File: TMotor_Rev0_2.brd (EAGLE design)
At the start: 106.7 x 74.3 mm, 86 parts, among them J1 5015680507, J10 5015680207, J2 5015680507, J7 5015680207, J8 5015680207, J9 5015680207, Q1 IRLB8721PBFTO220H, Q2 IRLB8721PBFTO220H, Q3 IRLB8721PBFTO220H, Q4 IRLB8721PBFTO220H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

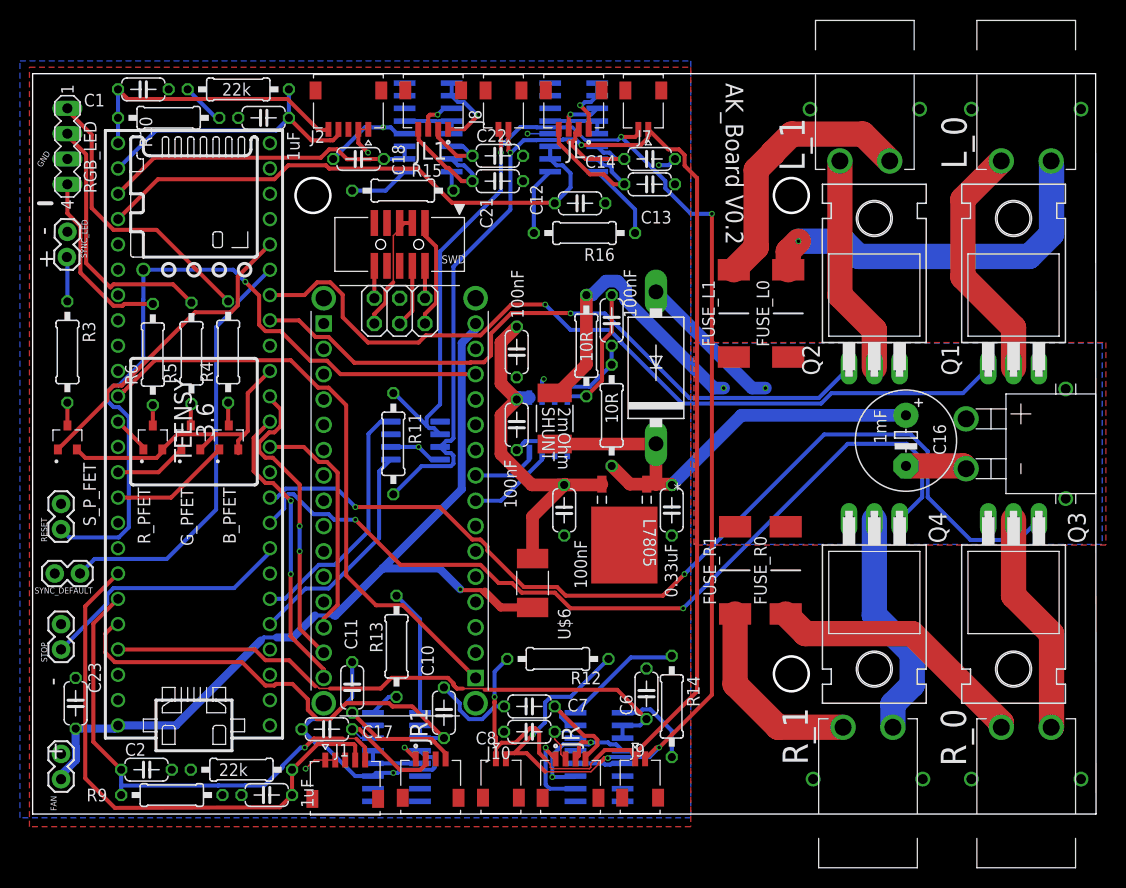
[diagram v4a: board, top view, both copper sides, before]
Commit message: Added Estop to motor power circuit
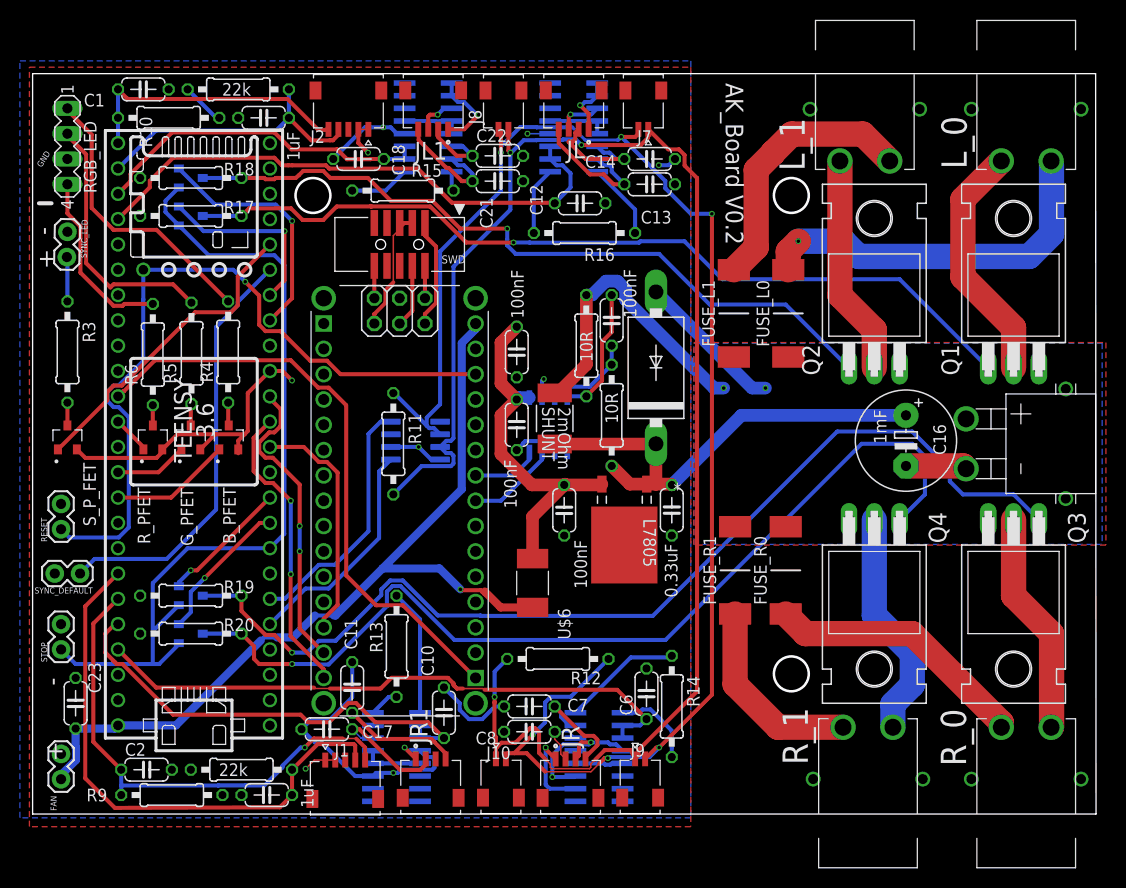
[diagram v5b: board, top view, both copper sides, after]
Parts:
- added R17, R18, R19, R20: 10R, rcl:0207/10
- added U6, U7, U8, U9: 2SJ305TE85LF, 2SJ305TE85LF:TRANS_SSM3J325F,LF
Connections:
- new net L0_ENABLE_STOP: Q1.1, R17.2, U6.3
- new net L1_ENABLE_STOP: Q2.1, R18.2, U7.3
- new net R0_ENABLE_STOP: Q3.1, R19.2, U8.3
- new net R1_ENABLE_STOP: Q4.1, R20.2, U9.3
- net GND: now also R17.1, R18.1, R19.1, R20.1
- net L_0_ENABLE: now also U6.2; no longer Q1.1
- net L_1_ENABLE: now also U7.2; no longer Q2.1
- net R_0_ENABLE: now also U8.2; no longer Q3.1
- net R_1_ENABLE: now also U9.2; no longer Q4.1
- net STOP: now also U6.1, U7.1, U8.1, U9.1
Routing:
- net R0_ENABLE_STOP: track 0.00 -> 104.0 mm, vias 0 -> 1
- net R1_ENABLE_STOP: track 0.00 -> 96.9 mm, vias 0 -> 1
- net L0_ENABLE_STOP: track 0.00 -> 87.1 mm, vias 0 -> 1
- net R_0_ENABLE: track 96.8 -> 13.0 mm, vias 2 -> 1
- net L1_ENABLE_STOP: track 0.00 -> 74.4 mm, vias 0 -> 1
- net R_1_ENABLE: track 86.5 -> 14.5 mm, vias 2 -> 1
- net L_0_ENABLE: track 83.7 -> 18.6 mm
- net STOP: track 25.9 -> 84.5 mm
- net L_1_ENABLE: track 68.0 -> 24.4 mm
- net TRQ_AMP_R1: track 69.0 -> 48.4 mm
- net 3.3V: track 62.1 -> 64.7 mm, vias 6 -> 7
- net TRQ_AMP_L1: track 32.3 -> 34.1 mm
- net TRQ_AMP_L: track 55.2 -> 56.2 mm
- net VIN: track 37.0 -> 36.4 mm

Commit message: Updated resistor value on motor stop pulldown
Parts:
- R17, R18: value 10R -> 1K
- R19, R20: value 10R -> 1k
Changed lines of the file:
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@@
 <attribute name="VALUE" x="-20.32" y="29.21" size="1.27" layer="28" rot="MR180"/>
 </element>
-<element name="R17" library="rcl" library_urn="urn:adsk.eagle:library:334" package="0207/10" package3d_urn="urn:adsk.eagle:package:23491/2" value="10R" x="-17.78" y="67.31" smashed="yes">
+<element name="R17" library="rcl" library_urn="urn:adsk.eagle:library:334" package="0207/10" package3d_urn="urn:adsk.eagle:package:23491/2" value="1K" x="-17.78" y="67.31" smashed="yes">
 <attribute name="NAME" x="-14.478" y="67.564" size="1.27" layer="25" ratio="10"/>
 <attribute name="POPULARITY" value="36" x="-17.78" y="67.31" size="1.778" layer="27" display="off"/>
@@
 <attribute name="VALUE" x="-20.0406" y="66.675" size="1.27" layer="27" ratio="10"/>
 </element>
-<element name="R18" library="rcl" library_urn="urn:adsk.eagle:library:334" package="0207/10" package3d_urn="urn:adsk.eagle:package:23491/2" value="10R" x="-17.78" y="71.12" smashed="yes">
+<element name="R18" library="rcl" library_urn="urn:adsk.eagle:library:334" package="0207/10" package3d_urn="urn:adsk.eagle:package:23491/2" value="1K" x="-17.78" y="71.12" smashed="yes">
 <attribute name="NAME" x="-14.478" y="71.374" size="1.27" layer="25" ratio="10"/>
 <attribute name="POPULARITY" value="36" x="-17.78" y="71.12" size="1.778" layer="27" display="off"/>
@@
 <attribute name="VALUE" x="-20.0406" y="70.485" size="1.27" layer="27" ratio="10"/>
 </element>
-<element name="R19" library="rcl" library_urn="urn:adsk.eagle:library:334" package="0207/10" package3d_urn="urn:adsk.eagle:package:23491/2" value="10R" x="-17.78" y="29.21" smashed="yes">
+<element name="R19" library="rcl" library_urn="urn:adsk.eagle:library:334" package="0207/10" package3d_urn="urn:adsk.eagle:package:23491/2" value="1k" x="-17.78" y="29.21" smashed="yes">
 <attribute name="NAME" x="-14.478" y="29.464" size="1.27" layer="25" ratio="10"/>
 <attribute name="POPULARITY" value="36" x="-17.78" y="29.21" size="1.778" layer="27" display="off"/>
@@
 <attribute name="VALUE" x="-20.0406" y="28.575" size="1.27" layer="27" ratio="10"/>
 </element>
-<element name="R20" library="rcl" library_urn="urn:adsk.eagle:library:334" package="0207/10" package3d_urn="urn:adsk.eagle:package:23491/2" value="10R" x="-17.78" y="25.4" smashed="yes">
+<element name="R20" library="rcl" library_urn="urn:adsk.eagle:library:334" package="0207/10" package3d_urn="urn:adsk.eagle:package:23491/2" value="1k" x="-17.78" y="25.4" smashed="yes">
 <attribute name="NAME" x="-14.478" y="25.654" size="1.27" layer="25" ratio="10"/>
 <attribute name="POPULARITY" value="36" x="-17.78" y="25.4" size="1.778" layer="27" display="off"/>

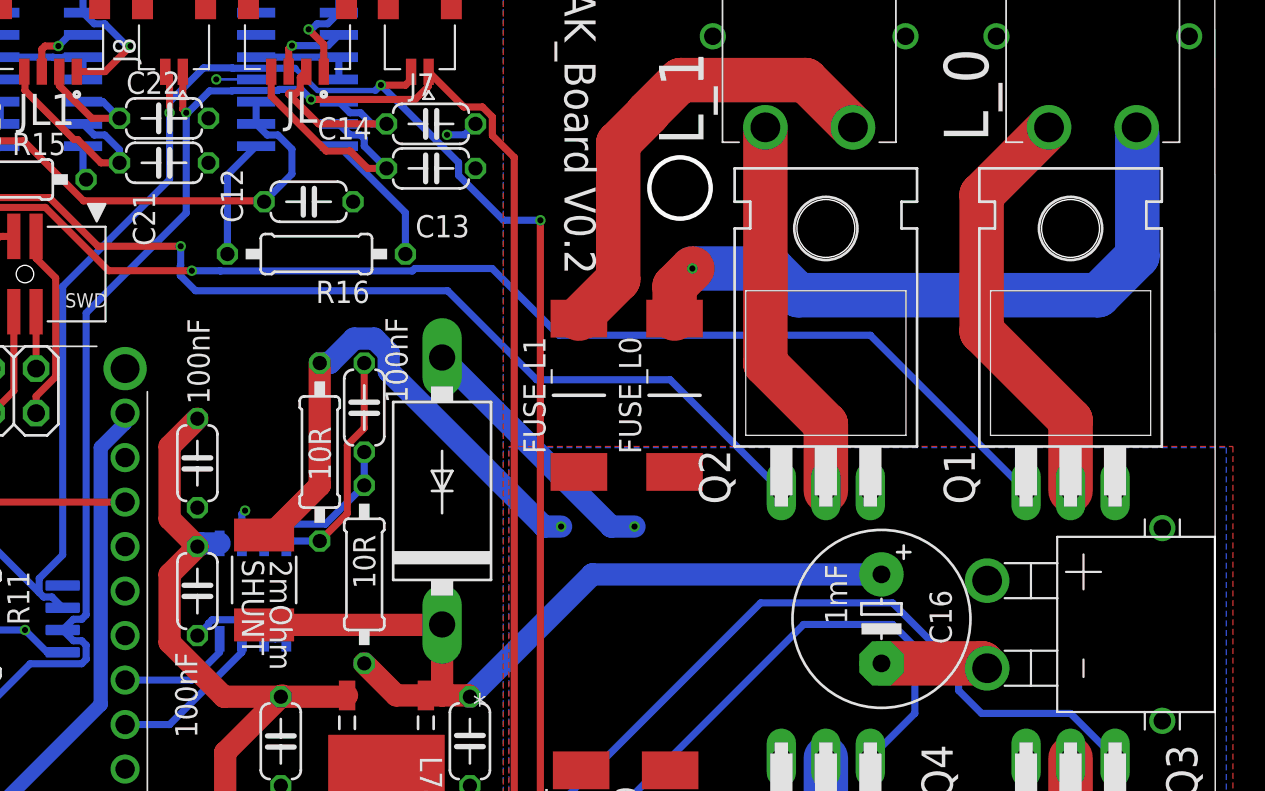
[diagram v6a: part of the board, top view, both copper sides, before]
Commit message: rerouted some traces for motor power
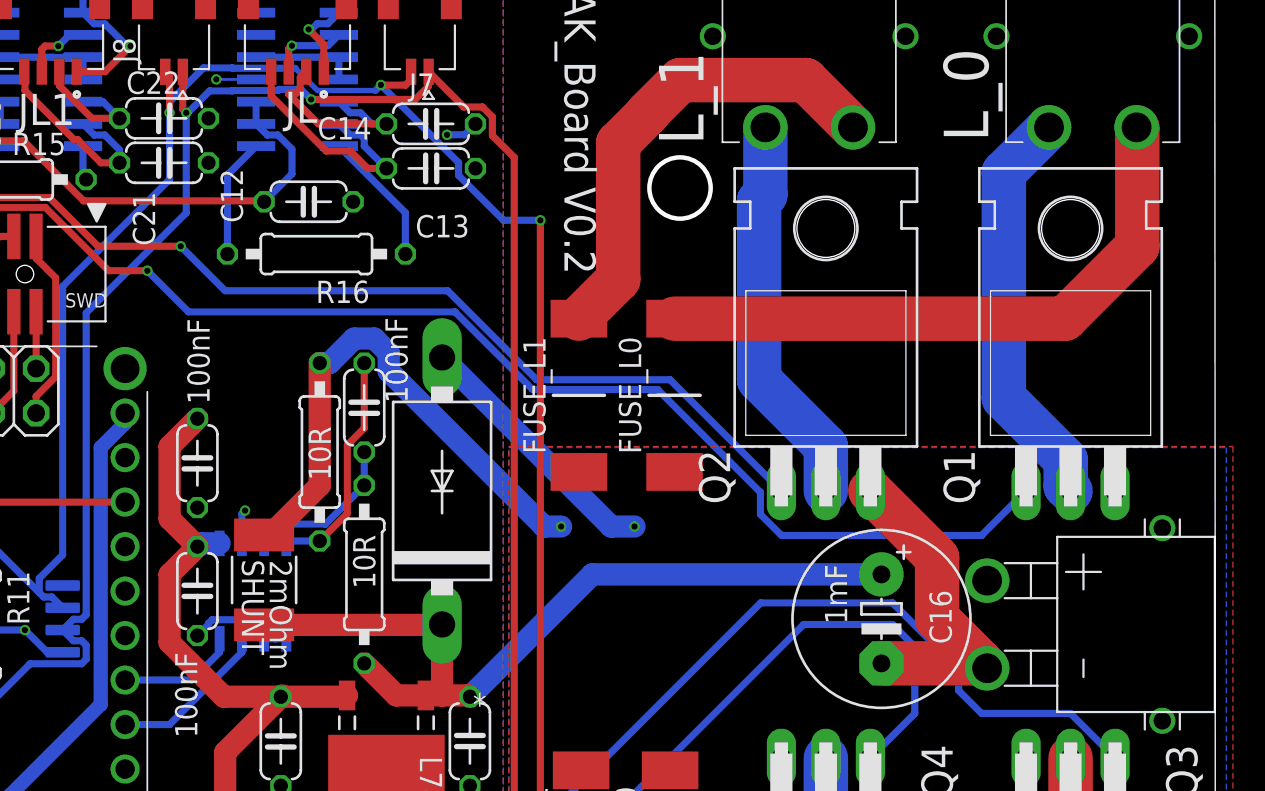
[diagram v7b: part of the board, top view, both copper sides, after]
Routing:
- net GND: track 112.6 -> 125.1 mm
- net L0_ENABLE_STOP: track 87.1 -> 89.8 mm
- net N$43: track 37.2 -> 34.9 mm, vias 1 -> 0
- net N$49: track 24.5 -> 23.4 mm
- net L1_ENABLE_STOP: track 74.4 -> 73.4 mm
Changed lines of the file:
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@@
 <contactref element="R18" pad="1"/>
 <contactref element="R17" pad="1"/>
+<wire x1="53.34" y1="52.07" x2="57.15" y2="48.26" width="2.54" layer="1"/>
+<wire x1="57.15" y1="44.8075" x2="59.73" y2="42.2275" width="2.54" layer="1"/>
+<wire x1="57.15" y1="48.26" x2="57.15" y2="44.8075" width="2.54" layer="1"/>
 <wire x1="-22.86" y1="67.31" x2="-22.86" y2="71.12" width="0" layer="19" extent="1-1"/>
 </signal>
@@
 <contactref element="L_0" pad="+"/>
 <contactref element="FUSE_L0" pad="2"/>
-<wire x1="42.164" y1="61.906" x2="42.164" y2="63.754" width="2.54" layer="1"/>
-<wire x1="42.164" y1="63.754" x2="43.18" y2="64.77" width="2.54" layer="1"/>
-<via x="43.18" y="64.77" extent="1-16" drill="0.35"/>
-<wire x1="43.18" y1="64.77" x2="47.69784375" y2="64.77" width="2.54" layer="16"/>
-<wire x1="47.69784375" y1="64.77" x2="49.22184375" y2="63.246" width="2.54" layer="16"/>
-<wire x1="66.34815625" y1="63.246" x2="68.58" y2="65.47784375" width="2.54" layer="16"/>
-<wire x1="68.58" y1="65.47784375" x2="68.58" y2="72.39" width="2.54" layer="16"/>
-<wire x1="49.22184375" y1="63.246" x2="66.34815625" y2="63.246" width="2.54" layer="16"/>
-<wire x1="68.58" y1="72.39" x2="68.54" y2="72.828" width="0" layer="19" extent="16-16"/>
+<wire x1="42.164" y1="61.906" x2="64.446" y2="61.906" width="2.54" layer="1"/>
+<wire x1="64.446" y1="61.906" x2="68.58" y2="66.04" width="2.54" layer="1"/>
+<wire x1="68.58" y1="66.04" x2="68.58" y2="72.788" width="2.54" layer="1"/>
+<wire x1="68.58" y1="72.788" x2="68.54" y2="72.828" width="2.54" layer="1"/>
 </signal>
 <signal name="N$46">
@@
 <contactref element="L_0" pad="-"/>
 <contactref element="Q1" pad="2"/>
-<wire x1="59.69" y1="68.978" x2="63.54" y2="72.828" width="2.54" layer="1"/>
-<wire x1="59.69" y1="61.185175" x2="59.69" y2="68.978" width="2.54" layer="1"/>
-<wire x1="59.69" y1="61.185175" x2="64.77" y2="56.105175" width="2.54" layer="1"/>
-<wire x1="64.77" y1="56.105175" x2="64.77" y2="52.07" width="2.54" layer="1"/>
+<wire x1="64.77" y1="52.07" x2="64.4906" y2="52.3494" width="2.54" layer="16"/>
+<wire x1="64.4906" y1="52.3494" x2="64.4906" y2="53.844575" width="2.54" layer="16"/>
+<wire x1="64.4906" y1="53.844575" x2="60.96" y2="57.375175" width="2.54" layer="16"/>
+<wire x1="60.96" y1="70.248" x2="63.54" y2="72.828" width="2.54" layer="16"/>
+<wire x1="60.96" y1="57.375175" x2="60.96" y2="70.248" width="2.54" layer="16"/>
 </signal>
 <signal name="N$50">
@@
 <contactref element="L_1" pad="-"/>
 <contactref element="Q2" pad="2"/>
-<wire x1="47.3475" y1="72.828" x2="47.3475" y2="59.3325" width="2.54" layer="1"/>
-<wire x1="47.3475" y1="59.3325" x2="50.8" y2="55.88" width="2.54" layer="1"/>
-<wire x1="50.8" y1="55.88" x2="50.8" y2="52.07" width="2.54" layer="1"/>
+<wire x1="50.8" y1="52.07" x2="50.8" y2="54.61" width="2.54" layer="16"/>
+<wire x1="46.99" y1="68.63415625" x2="47.3475" y2="68.99165625" width="2.54" layer="16"/>
+<wire x1="47.3475" y1="68.99165625" x2="47.3475" y2="72.828" width="2.54" layer="16"/>
+<wire x1="46.99" y1="58.42" x2="46.99" y2="68.63415625" width="2.54" layer="16"/>
+<wire x1="50.8" y1="54.61" x2="46.99" y2="58.42" width="2.54" layer="16"/>
 </signal>
 <signal name="L_0_ENABLE">
@@
 <contactref element="R17" pad="2"/>
 <wire x1="-16.58" y1="67.31" x2="-12.7" y2="67.31" width="0.4064" layer="16"/>
-<wire x1="62.23" y1="52.07" x2="53.34" y2="60.96" width="0.4064" layer="16"/>
-<wire x1="35.56" y1="60.96" x2="31.75" y2="64.77" width="0.4064" layer="16"/>
-<via x="14.605" y="64.643" extent="1-16" drill="0.35"/>
-<wire x1="31.75" y1="64.77" x2="27.3365" y2="64.77" width="0.4064" layer="16"/>
-<wire x1="27.3365" y1="64.77" x2="27.1968" y2="64.6303" width="0.4064" layer="16"/>
-<wire x1="16.2372" y1="64.6303" x2="16.2245" y2="64.643" width="0.4064" layer="16"/>
-<wire x1="16.2245" y1="64.643" x2="14.605" y2="64.643" width="0.4064" layer="16"/>
-<wire x1="27.1968" y1="64.6303" x2="16.2372" y2="64.6303" width="0.4064" layer="16"/>
+<via x="12.065" y="64.643" extent="1-16" drill="0.35"/>
 <wire x1="0.3219" y1="68.2581" x2="0.254" y2="68.326" width="0.4064" layer="1"/>
 <wire x1="6.24229375" y1="68.2581" x2="0.3219" y2="68.2581" width="0.4064" layer="1"/>
-<wire x1="14.605" y1="64.643" x2="9.85739375" y2="64.643" width="0.4064" layer="1"/>
+<wire x1="12.065" y1="64.643" x2="9.85739375" y2="64.643" width="0.4064" layer="1"/>
 <wire x1="9.85739375" y1="64.643" x2="6.24229375" y2="68.2581" width="0.4064" layer="1"/>
-<wire x1="53.34" y1="60.96" x2="35.56" y2="60.96" width="0.4064" layer="16"/>
 <wire x1="0.3219" y1="68.2581" x2="-3.13794375" y2="68.2581" width="0.4064" layer="1"/>
 <wire x1="-7.72595625" y1="68.072" x2="-11.938" y2="68.072" width="0.4064" layer="1"/>
@@
 <wire x1="-4.49224375" y1="66.9038" x2="-6.55775625" y2="66.9038" width="0.4064" layer="1"/>
 <wire x1="-6.55775625" y1="66.9038" x2="-7.72595625" y2="68.072" width="0.4064" layer="1"/>
+<wire x1="12.065" y1="64.643" x2="14.4145" y2="62.2935" width="0.4064" layer="16"/>
+<wire x1="29.62623125" y1="62.2935" x2="34.05853125" y2="57.8612" width="0.4064" layer="16"/>
+<wire x1="34.05853125" y1="57.8612" x2="41.1988" y2="57.8612" width="0.4064" layer="16"/>
+<wire x1="47.0662" y1="51.9938" x2="47.0662" y2="50.73730625" width="0.4064" layer="16"/>
+<wire x1="47.0662" y1="50.73730625" x2="48.27350625" y2="49.53" width="0.4064" layer="16"/>
+<wire x1="59.69" y1="49.53" x2="62.23" y2="52.07" width="0.4064" layer="16"/>
+<wire x1="14.4145" y1="62.2935" x2="29.62623125" y2="62.2935" width="0.4064" layer="16"/>
+<wire x1="41.1988" y1="57.8612" x2="47.0662" y2="51.9938" width="0.4064" layer="16"/>
+<wire x1="48.27350625" y1="49.53" x2="59.69" y2="49.53" width="0.4064" layer="16"/>
 </signal>
 <signal name="L1_ENABLE_STOP">
@@
 <wire x1="-16.58" y1="71.12" x2="-12.7" y2="71.12" width="0.4064" layer="16"/>
 <wire x1="48.26" y1="52.07" x2="41.91" y2="58.42" width="0.4064" layer="16"/>
-<wire x1="13.9474" y1="64.3706125" x2="13.9474" y2="64.9153875" width="0.4064" layer="16"/>
-<wire x1="13.9474" y1="64.9153875" x2="13.97" y2="64.9379875" width="0.4064" layer="16"/>
-<wire x1="13.97" y1="64.9379875" x2="13.97" y2="66.04" width="0.4064" layer="16"/>
 <via x="13.97" y="66.04" extent="1-16" drill="0.35"/>
 <wire x1="13.97" y1="66.04" x2="9.2506625" y2="66.04" width="0.4064" layer="1"/>
@@
 <wire x1="-10.41664375" y1="71.12" x2="-12.7" y2="71.12" width="0.4064" layer="1"/>
 <wire x1="41.91" y1="58.42" x2="34.29" y2="58.42" width="0.4064" layer="16"/>
-<wire x1="34.29" y1="58.42" x2="29.21" y2="63.5" width="0.4064" layer="16"/>
-<wire x1="29.21" y1="63.5" x2="14.8180125" y2="63.5" width="0.4064" layer="16"/>
-<wire x1="14.8180125" y1="63.5" x2="13.9474" y2="64.3706125" width="0.4064" layer="16"/>
+<wire x1="29.21" y1="63.5" x2="34.29" y2="58.42" width="0.4064" layer="16"/>
 <wire x1="-7.26241875" y1="71.12" x2="-9.26835625" y2="71.12" width="0.4064" layer="1"/>
+<wire x1="13.97" y1="66.04" x2="16.51" y2="63.5" width="0.4064" layer="16"/>
+<wire x1="16.51" y1="63.5" x2="29.21" y2="63.5" width="0.4064" layer="16"/>
 </signal>
 <signal name="R0_ENABLE_STOP">
